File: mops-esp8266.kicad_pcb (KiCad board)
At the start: 2 copper layers, 56.5 x 53.5 mm, 43 parts, among them J1 USB_B_Micro, J2 PMS7003, J3 Ext_I2C, Q1 BC560, SW1 SW_Flash, U1 AP1117-33, U2 ESP-12F, U3 SHT31-DIS, U4 BME280, U5 CH330N

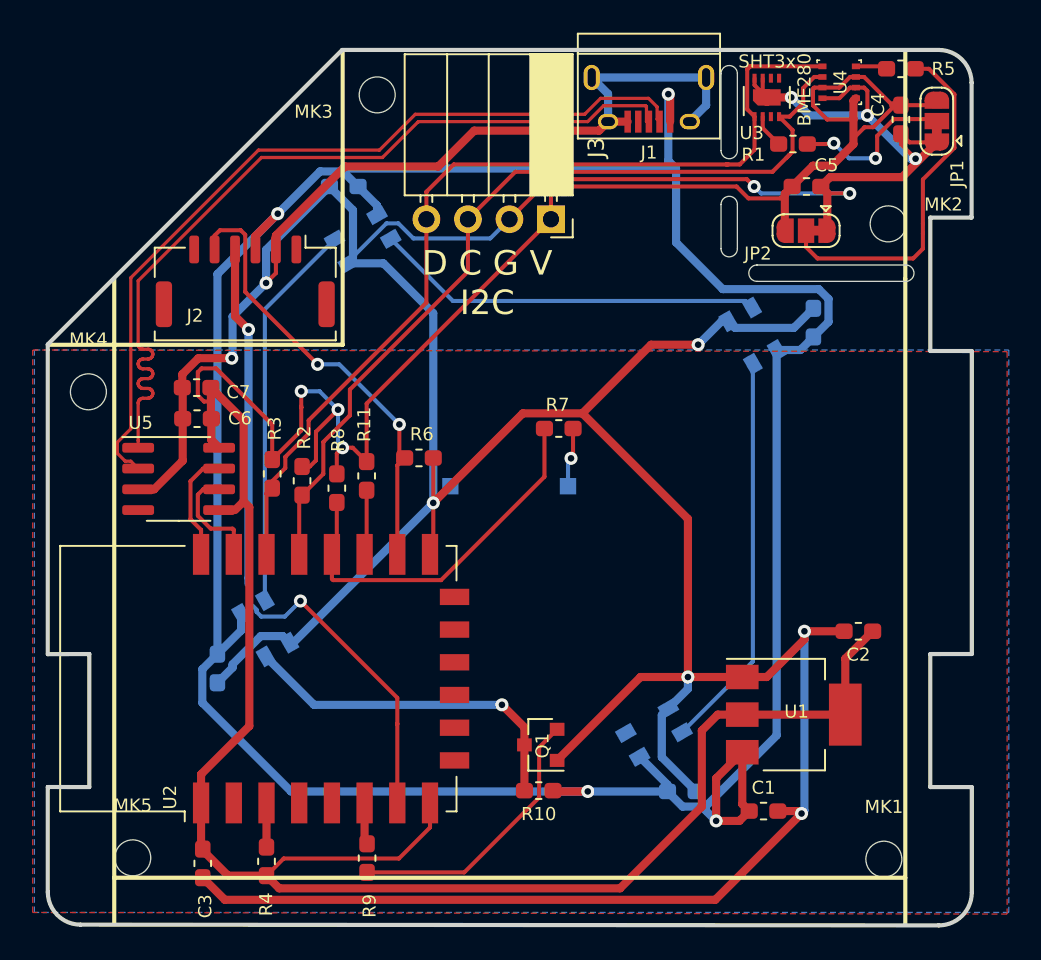
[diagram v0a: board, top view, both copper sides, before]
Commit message: WIP: Add a place to solde ESP12F on the back
Signed-off-by: Zamir SUN <sztsian@gmail.com>
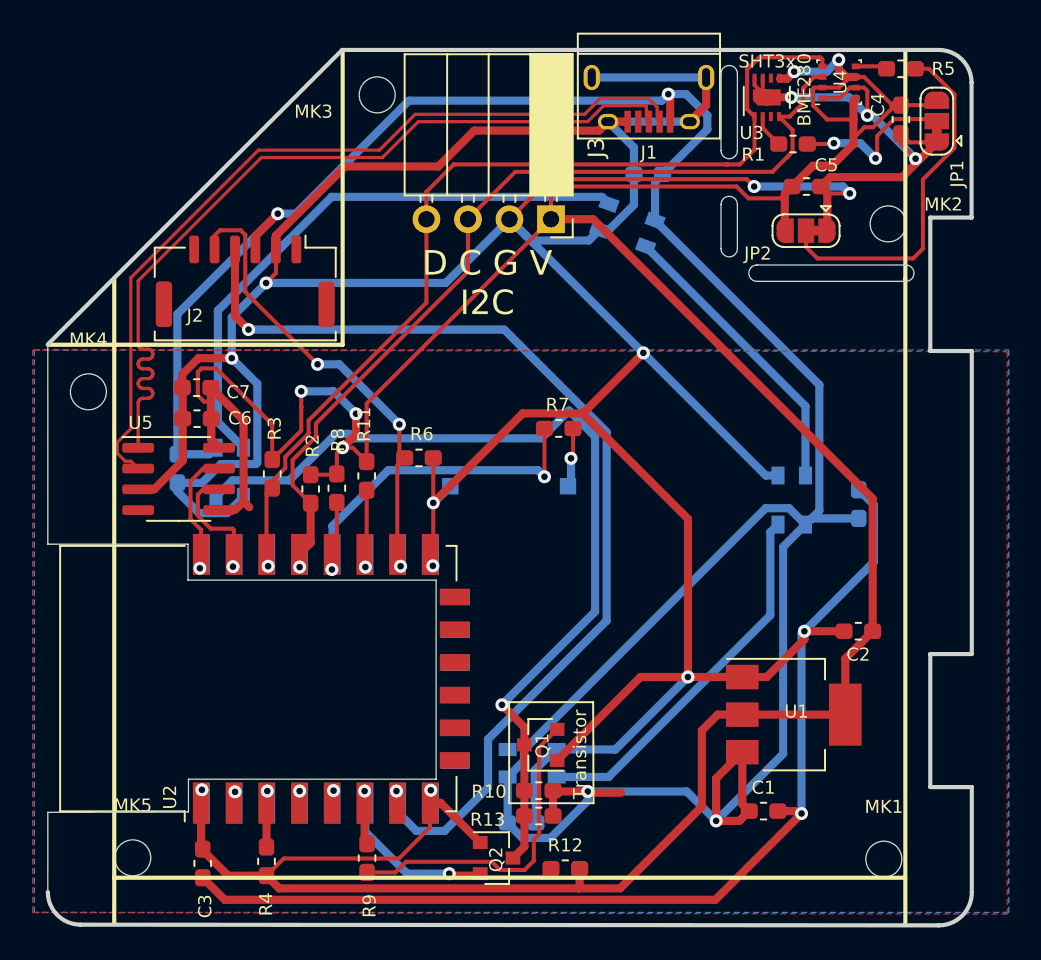
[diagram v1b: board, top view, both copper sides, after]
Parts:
- added Q2: 2N7002E/AO3400, Package_TO_SOT_SMD:SOT-23, F.Cu at (59.1, 131.8)
- added R12: 10k, Resistor_SMD:R_0603_1608Metric_Pad1.05x0.95mm_HandSolder, F.Cu at (63.3, 132.4)
- added R13: 10k, Resistor_SMD:R_0603_1608Metric_Pad1.05x0.95mm_HandSolder, F.Cu at (61.6, 129.2)
- added U6: ESP-12F, RF_Module:ESP-12E, B.Cu at (43.7, 120.7)
- C2: value 100uF -> 100nF
- moved C9 18.6 mm to (68.3, 90.0)
- moved D2 16.2 mm to (67.1, 93.1), turned to 160 degrees
- moved C8 12.5 mm to (39.5, 108.0)
- moved C10 11.4 mm to (81.2, 110.1)
- moved D3 10.3 mm to (77.1, 109.9), turned to 90 degrees
- moved C11 9.98 mm to (60.6, 129.6)
- moved D1 9.79 mm to (42.8, 108.2), turned to 270 degrees
- moved D4 7.68 mm to (61.2, 126.0), turned to 0 degrees
- moved R2 0.73 mm to (47.7, 109.2)
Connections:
- net Net-(D1-Pad4) renamed WS_IN
- net Net-(R4-Pad1) renamed EN
- U2 pad 2: (no net) -> A0
- U2 pad 4: (no net) -> GPIO16
- U2 pad 5: (no net) -> GPIO14
- U3 pad 5: (no net) -> 3V3_MCU
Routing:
- net WS_IN: track 21.5 -> 55.3 mm
- net 3V3_MCU: track 195.7 -> 220.6 mm, vias 3 -> 7
- net GPIO13: track 41.1 -> 62.1 mm
- net GND: track 313.6 -> 332.4 mm, vias 12 -> 13
- net GPIO12: track 2.56 -> 17.1 mm, vias 0 -> 2
- net Net-(D1-Pad2): track 23.8 -> 37.0 mm
- net Net-(D2-Pad2): track 23.8 -> 18.1 mm
- net VBUS: track 173.9 -> 169.8 mm
- net Net-(Q1-Pad2): track 17.0 -> 19.5 mm
- net Net-(D3-Pad2): track 24.3 -> 22.9 mm
- net GPIO4: track 53.3 -> 54.2 mm, vias 0 -> 1
- net GPIO5: track 57.3 -> 58.0 mm, vias 0 -> 1
- net GPIO0: track 23.4 -> 23.5 mm, vias 0 -> 2
- net IF_TXD: vias 0 -> 1
- net IF_RXD: vias 0 -> 1
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- added copper zone on B.Cu, net 3V3_MCU
- removed copper zone on B.Cu, net VBUS
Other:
- outline, holes or cut-outs redrawn
- board text added: "Transistor"

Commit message: Upload v0.2. Still not working.
Size of PCB is too large on the buttom size
ESP modules should move right a bit
D2 should move down a bit
Temperature sensor can be removed as the self heating affects it too
much

Signed-off-by: Zamir SUN <sztsian@gmail.com>
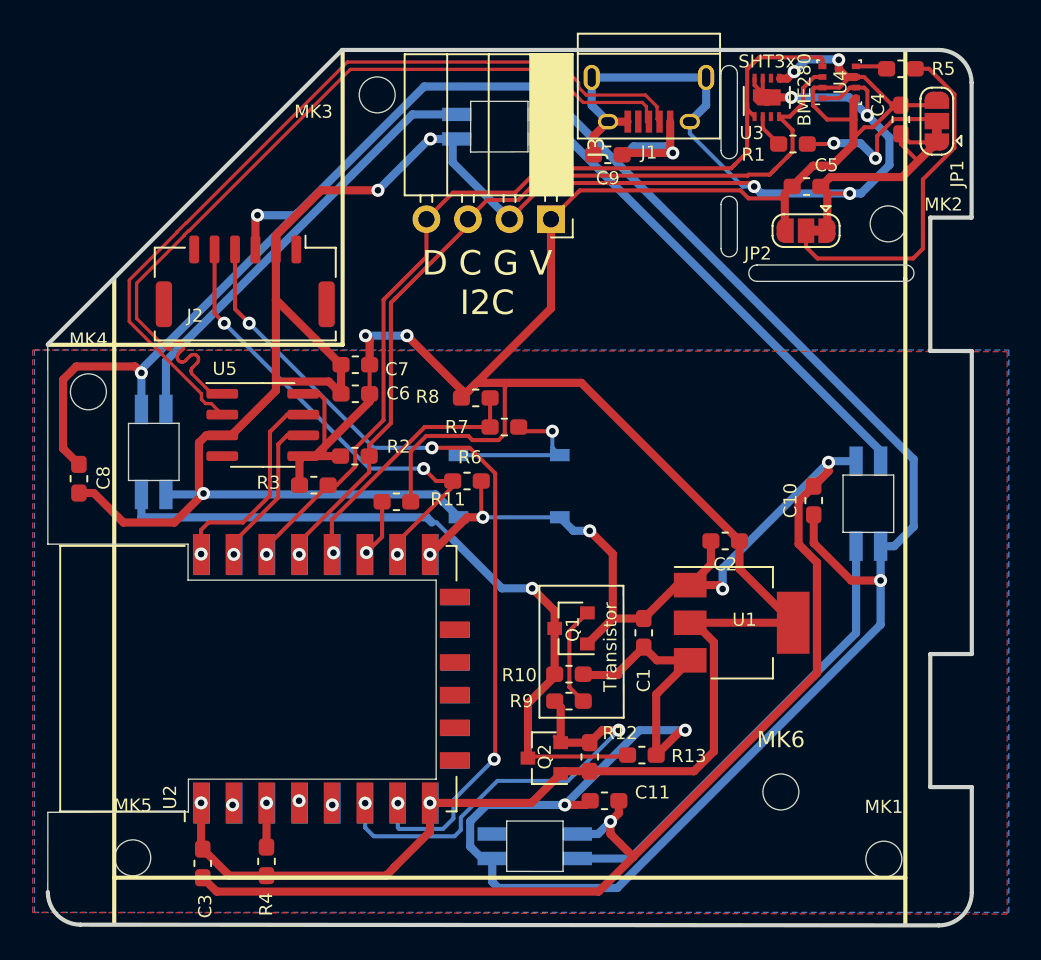
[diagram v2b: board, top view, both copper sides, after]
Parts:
- added MK6: M1, MountingHole:MountingHole_2.2mm_M2, F.Cu at (76.5, 127.7)
- C10, C11, C8, C9: moved to F.Cu
- D1, D2, D3, D4: footprint zsun-symbols:LED_WS2812B_3.5x3.5mm -> zsun-symbols:LED_DY-S352818_RGBC_6812-2T
- SW1: footprint w_switch:smd_push -> zsun-symbols:switch_4x4x1.5_real-5x5x1.5
- moved R9 15.6 mm to (63.5, 122.2), turned to 0 degrees
- moved C1 13.1 mm to (68.1, 118.0), turned to 90 degrees
- moved R8 10.1 mm to (57.8, 103.6), turned to 0 degrees
- moved D2 9.88 mm to (59.2, 87.0), turned to 180 degrees
- moved C2 9.84 mm to (73.1, 112.4)
- moved C7 9.81 mm to (50.4, 101.6)
- moved C6 9.80 mm to (50.4, 103.4)
- moved R10 7.36 mm to (63.5, 120.5)
- moved Q1 7.36 mm to (63.6, 117.7)
- moved R13 7.33 mm to (68.0, 125.5)
- moved R12 7.00 mm to (64.8, 125.6), turned to 270 degrees
- moved Q2 6.77 mm to (62.0, 125.7), turned to 180 degrees
- moved U1 6.46 mm to (74.1, 117.4)
- moved U5 6.11 mm to (44.8, 105.3)
- moved C8 6.05 mm to (33.5, 108.6)
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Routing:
- net GND: track 332.4 -> 271.5 mm
- net 3V3_MCU: track 220.6 -> 184.8 mm, vias 7 -> 6
- net Net-(Q1-Pad2): track 19.5 -> 6.21 mm
- net Net-(D2-Pad2): track 18.1 -> 29.2 mm
- net GPIO13: track 62.1 -> 51.1 mm, vias 2 -> 4
- net GPIO12: track 17.1 -> 28.0 mm
- net WS_IN: track 55.3 -> 45.0 mm
- net VBUS: track 169.8 -> 179.9 mm, vias 4 -> 6
- net Net-(D1-Pad2): track 37.0 -> 27.0 mm
- net Net-(R7-Pad1): track 3.66 -> 9.92 mm
- net IF_RXD: track 6.82 -> 12.9 mm
- net Net-(D3-Pad2): track 22.9 -> 28.1 mm
- net GPIO0: track 23.5 -> 18.8 mm, vias 2 -> 1
- net IF_TXD: track 6.78 -> 9.61 mm
- net GPIO15: track 27.5 -> 28.6 mm
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- added copper zone on B.Cu, net VBUS
- removed copper zone on B.Cu, net 3V3_MCU
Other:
- outline, holes or cut-outs redrawn
- board text added: "v0.2"
- board text removed: "v0.1"

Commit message: Update to v0.3
Fixes board size and position in various places
Removed temperature sensor

Signed-off-by: Zamir SUN <sztsian@gmail.com>
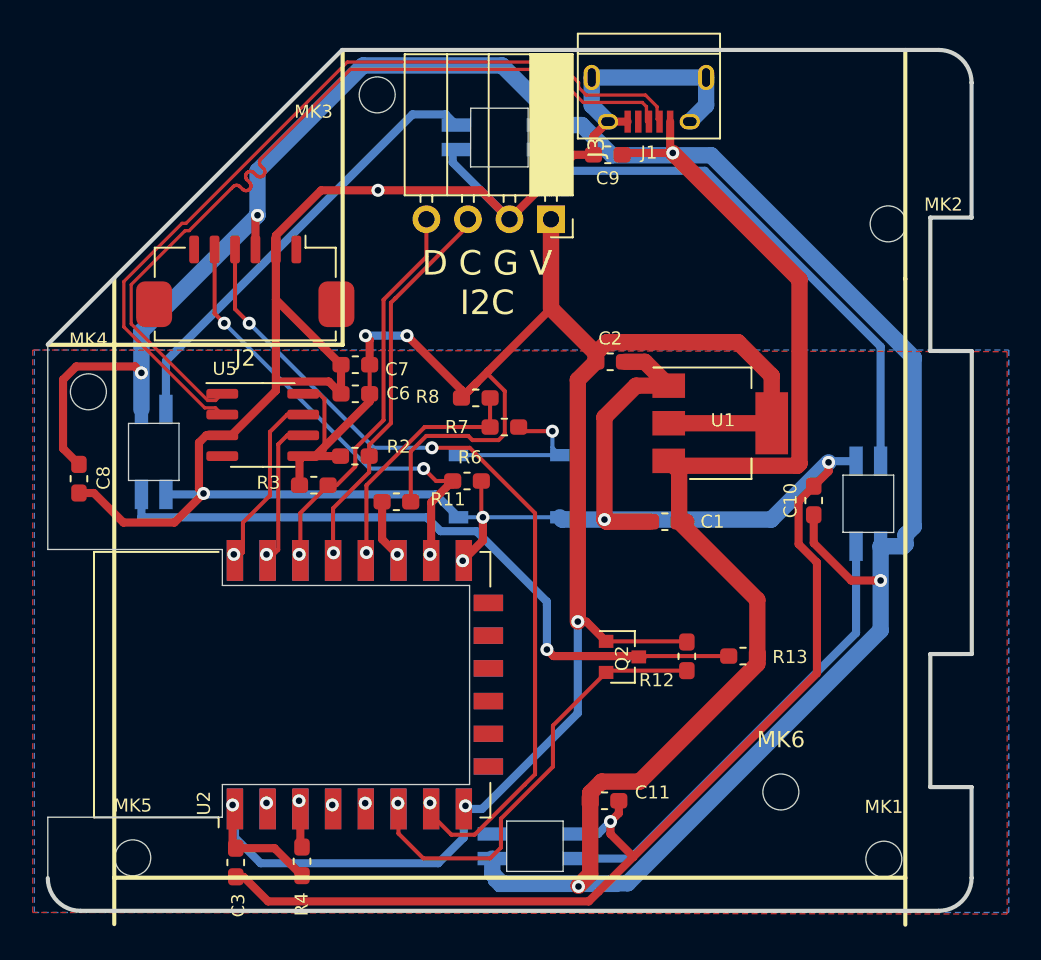
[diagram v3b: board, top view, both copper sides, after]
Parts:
- removed C4, C5: 100nF, Capacitor_SMD:C_0603_1608Metric_Pad1.05x0.95mm_HandSolder
- removed JP1, JP2: SJ_Addr, Jumper:SolderJumper-3_P1.3mm_Bridged12_RoundedPad1.0x1.5mm
- removed Q1: BC560, Package_TO_SOT_SMD:SOT-23
- removed R1, R5: 10k, Resistor_SMD:R_0603_1608Metric_Pad1.05x0.95mm_HandSolder
- removed R10: 1k8, Resistor_SMD:R_0603_1608Metric_Pad1.05x0.95mm_HandSolder
- removed R9: 3k3, Resistor_SMD:R_0603_1608Metric_Pad1.05x0.95mm_HandSolder
- removed U3: SHT31-DIS, mops-esp8266:Sensirion_DFN-8-1EP_2.5x2.5mm_P0.5mm_EP1.1x1.7mm
- removed U4: BME280, Package_LGA:Bosch_LGA-8_2.5x2.5mm_P0.65mm_ClockwisePinNumbering
- J2: footprint Connector_Molex:Molex_CLIK-Mate_502382-0670_1x06-1MP_P1.25mm_Vertical -> zsun-connectors:1.25mm_connector_Vertical-based-on-molex-502382-1x06
- Q2: value 2N7002E/AO3400 -> 2N7002
- R12, R13: value 10k -> 1k
- moved C2 13.0 mm to (66.0, 101.4), turned to 0 degrees
- moved U1 12.3 mm to (72.8, 105.2)
- moved R13 8.66 mm to (74.1, 119.4)
- moved R12 8.55 mm to (70.7, 119.4), turned to 90 degrees
- moved Q2 7.82 mm to (66.8, 119.5), turned to 0 degrees
- moved C1 6.92 mm to (69.4, 111.2), turned to 180 degrees
- moved R4 2.17 mm to (47.2, 132.0)
- moved U2 2.10 mm to (46.6, 121.2)
- moved U6 2.07 mm to (45.7, 121.1)
- moved C3 2.02 mm to (43.1, 132.0)
- moved D2 0.65 mm to (59.2, 87.7)
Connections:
- net WS_IN renamed Net-(D1-Pad4)
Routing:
- net VBUS: track 179.9 -> 276.1 mm, vias 6 -> 5
- net GND: track 271.5 -> 214.8 mm, vias 13 -> 7
- net 3V3_MCU: track 184.8 -> 146.0 mm, vias 6 -> 5
- net GPIO5: track 57.8 -> 25.1 mm
- net GPIO4: track 53.6 -> 25.6 mm
- net Net-(JP2-Pad2): track 22.0 -> 0.00 mm
- net Net-(JP1-Pad2): track 10.1 -> 0.00 mm, vias 2 -> 0
- net Net-(Q1-Pad2): track 6.21 -> 0.00 mm
- net Net-(D2-Pad2): track 29.2 -> 33.9 mm
- net GPIO0: track 18.8 -> 15.1 mm
- net Net-(D1-Pad4): track 45.0 -> 42.9 mm
- net Net-(R1-Pad2): track 2.08 -> 0.00 mm
- net Net-(R5-Pad2): track 1.94 -> 0.00 mm
- net USB-D+: track 50.9 -> 52.1 mm
- net GPIO13: track 51.1 -> 52.3 mm, vias 4 -> 3
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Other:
- board size 56.5 x 53.5 mm -> 56.5 x 52.7 mm
- board text added: "v0.3"
- board text removed: "BME280"
- board text removed: "SHT3x"
- board text removed: "Transistor"
- board text removed: "v0.2"
